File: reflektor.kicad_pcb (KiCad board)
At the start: 2 copper layers, 94 x 94 mm, 4 parts, among them J1 Conn_01x01_Male

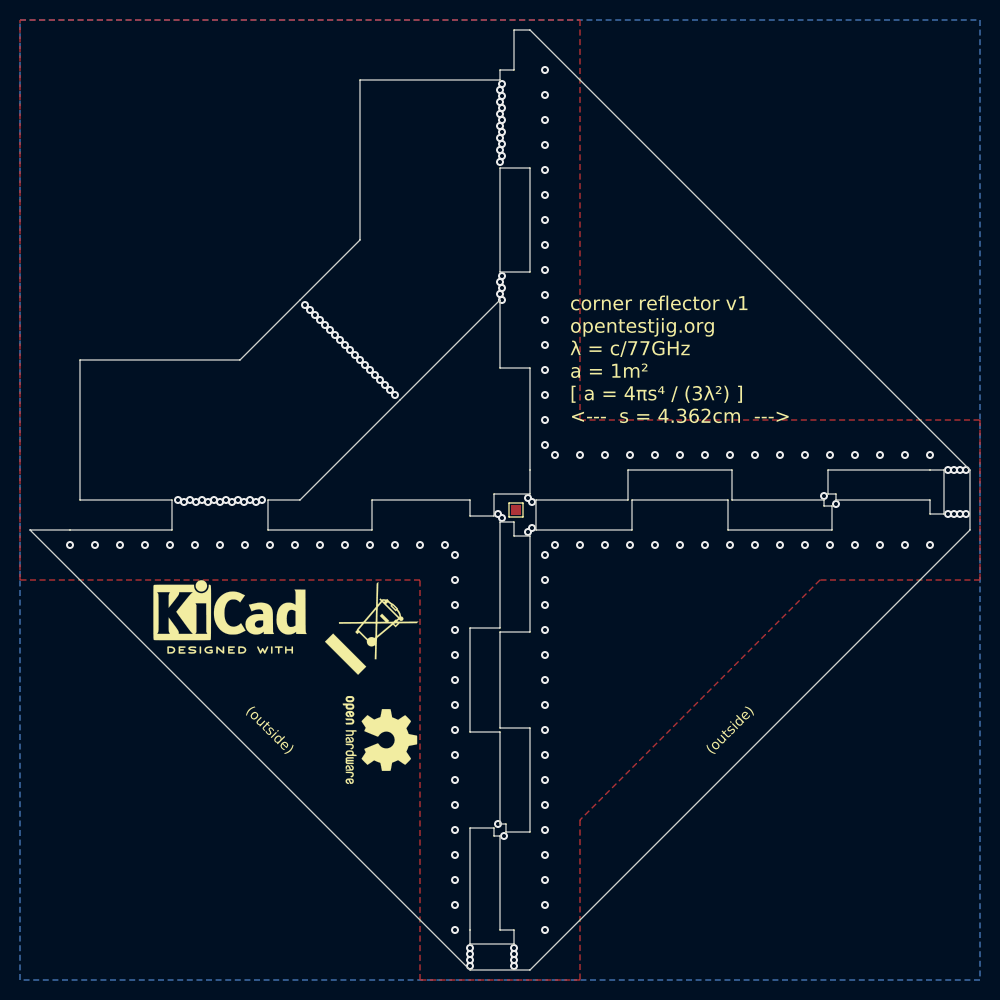
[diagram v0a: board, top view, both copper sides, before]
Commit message: version 2: increase board-connections to at least 4mm
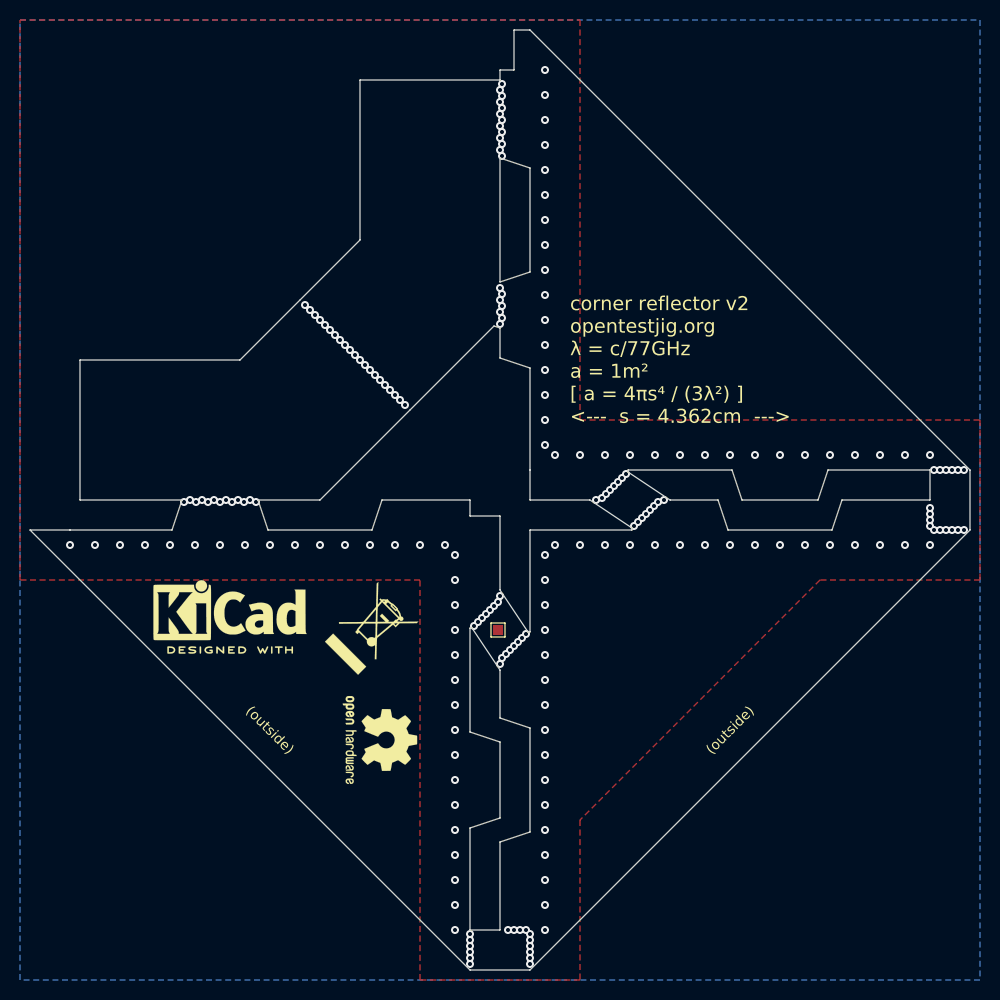
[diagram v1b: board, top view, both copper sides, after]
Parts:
- moved J1 12.1 mm to (66.8, 76.0)
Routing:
- net GND: vias 175 -> 214
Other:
- outline, holes or cut-outs redrawn
- board text added: "corner reflector v2 opentestjig.org λ = c/77GHz a = 1m² [ a = 4πs⁴ / (3λ²) ] <--- s = 4.362cm --->"
- board text removed: "corner reflector v1 opentestjig.org λ = c/77GHz a = 1m² [ a = 4πs⁴ / (3λ²) ] <--- s = 4.362cm --->"
